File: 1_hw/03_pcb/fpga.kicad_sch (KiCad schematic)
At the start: 18 parts, among them U2 ICE40UP5K-SG48ITR

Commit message: FEAT: Added Connectors on Schematic. Created Connector Footprints.
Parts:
- gave numbers to parts that had none: 17
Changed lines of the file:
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@@
 		(on_board yes)
 		(dnp no)
-		(property "Reference" "C?"
+		(property "Reference" "C79"
 			(at 146.05 92.7162 0)
 			(effects
@@
 			(project "arb"
 				(path "/866ef9be-3b01-4288-a6e0-a2357aa17e50/13f127a8-adf3-43db-9fea-9a9f154787f6"
-					(reference "C?")
+					(reference "C79")
 					(unit 1)
 				)
@@
 		(dnp no)
 		(fields_autoplaced yes)
-		(property "Reference" "C?"
+		(property "Reference" "C84"
 			(at 180.34 78.7462 0)
 			(effects
@@
 			(project "arb"
 				(path "/866ef9be-3b01-4288-a6e0-a2357aa17e50/13f127a8-adf3-43db-9fea-9a9f154787f6"
-					(reference "C?")
+					(reference "C84")
 					(unit 1)
 				)
@@
 		(dnp no)
 		(fields_autoplaced yes)
-		(property "Reference" "U?"
+		(property "Reference" "U14"
 			(at 248.92 147.3199 0)
 			(effects
@@
 			(project ""
 				(path "/866ef9be-3b01-4288-a6e0-a2357aa17e50/13f127a8-adf3-43db-9fea-9a9f154787f6"
-					(reference "U?")
+					(reference "U14")
 					(unit 1)
 				)
@@
 		(dnp no)
 		(fields_autoplaced yes)
-		(property "Reference" "C?"
+		(property "Reference" "C81"
 			(at 170.18 78.7462 0)
 			(effects
@@
 			(project "arb"
 				(path "/866ef9be-3b01-4288-a6e0-a2357aa17e50/13f127a8-adf3-43db-9fea-9a9f154787f6"
-					(reference "C?")
+					(reference "C81")
 					(unit 1)
 				)
@@
 		(dnp no)
 		(fields_autoplaced yes)
-		(property "Reference" "C?"
+		(property "Reference" "C76"
 			(at 100.33 26.6762 0)
 			(effects
@@
 			(project "arb"
 				(path "/866ef9be-3b01-4288-a6e0-a2357aa17e50/13f127a8-adf3-43db-9fea-9a9f154787f6"
-					(reference "C?")
+					(reference "C76")
 					(unit 1)
 				)
@@
 		(on_board yes)
 		(dnp no)
-		(property "Reference" "R?"
+		(property "Reference" "R44"
 			(at 219.202 135.636 0)
 			(effects
@@
 			(project "arb"
 				(path "/866ef9be-3b01-4288-a6e0-a2357aa17e50/13f127a8-adf3-43db-9fea-9a9f154787f6"
-					(reference "R?")
+					(reference "R44")
 					(unit 1)
 				)
@@
 		(dnp no)
 		(fields_autoplaced yes)
-		(property "Reference" "C?"
+		(property "Reference" "C80"
 			(at 163.83 26.6762 0)
 			(effects
@@
 			(project "arb"
 				(path "/866ef9be-3b01-4288-a6e0-a2357aa17e50/13f127a8-adf3-43db-9fea-9a9f154787f6"
-					(reference "C?")
+					(reference "C80")
 					(unit 1)
 				)
@@
 		(on_board yes)
 		(dnp no)
-		(property "Reference" "C?"
+		(property "Reference" "C78"
 			(at 135.89 92.7162 0)
 			(effects
@@
 			(project "arb"
 				(path "/866ef9be-3b01-4288-a6e0-a2357aa17e50/13f127a8-adf3-43db-9fea-9a9f154787f6"
-					(reference "C?")
+					(reference "C78")
 					(unit 1)
 				)
@@
 		(dnp no)
 		(fields_autoplaced yes)
-		(property "Reference" "R?"
+		(property "Reference" "R42"
 			(at 182.88 83.82 90)
 			(effects
@@
 			(project "arb"
 				(path "/866ef9be-3b01-4288-a6e0-a2357aa17e50/13f127a8-adf3-43db-9fea-9a9f154787f6"
-					(reference "R?")
+					(reference "R42")
 					(unit 1)
 				)
@@
 		(dnp no)
 		(fields_autoplaced yes)
-		(property "Reference" "C?"
+		(property "Reference" "C74"
 			(at 90.17 26.6762 0)
 			(effects
@@
 			(project "arb"
 				(path "/866ef9be-3b01-4288-a6e0-a2357aa17e50/13f127a8-adf3-43db-9fea-9a9f154787f6"
-					(reference "C?")
+					(reference "C74")
 					(unit 1)
 				)
@@
 		(dnp no)
 		(fields_autoplaced yes)
-		(property "Reference" "C?"
+		(property "Reference" "C82"
 			(at 170.18 92.7162 0)
 			(effects
@@
 			(project "arb"
 				(path "/866ef9be-3b01-4288-a6e0-a2357aa17e50/13f127a8-adf3-43db-9fea-9a9f154787f6"
-					(reference "C?")
+					(reference "C82")
 					(unit 1)
 				)
@@
 		(on_board yes)
 		(dnp no)
-		(property "Reference" "R?"
+		(property "Reference" "R43"
 			(at 210.312 135.636 0)
 			(effects
@@
 			(project "arb"
 				(path "/866ef9be-3b01-4288-a6e0-a2357aa17e50/13f127a8-adf3-43db-9fea-9a9f154787f6"
-					(reference "R?")
+					(reference "R43")
 					(unit 1)
 				)
@@
 		(dnp no)
 		(fields_autoplaced yes)
-		(property "Reference" "C?"
+		(property "Reference" "C86"
 			(at 247.65 128.2763 0)
 			(effects
@@
 			(project "arb"
 				(path "/866ef9be-3b01-4288-a6e0-a2357aa17e50/13f127a8-adf3-43db-9fea-9a9f154787f6"
-					(reference "C?")
+					(reference "C86")
 					(unit 1)
 				)
@@
 		(dnp no)
 		(fields_autoplaced yes)
-		(property "Reference" "C?"
+		(property "Reference" "C85"
 			(at 180.34 92.7162 0)
 			(effects
@@
 			(project "arb"
 				(path "/866ef9be-3b01-4288-a6e0-a2357aa17e50/13f127a8-adf3-43db-9fea-9a9f154787f6"
-					(reference "C?")
+					(reference "C85")
 					(unit 1)
 				)
@@
 		(dnp no)
 		(fields_autoplaced yes)
-		(property "Reference" "C?"
+		(property "Reference" "C75"
 			(at 91.44 104.1462 0)
 			(effects
@@
 			(project "arb"
 				(path "/866ef9be-3b01-4288-a6e0-a2357aa17e50/13f127a8-adf3-43db-9fea-9a9f154787f6"
-					(reference "C?")
+					(reference "C75")
 					(unit 1)
 				)
@@
 		(dnp no)
 		(fields_autoplaced yes)
-		(property "Reference" "C?"
+		(property "Reference" "C83"
 			(at 173.99 26.6762 0)
 			(effects
@@
 			(project "arb"
 				(path "/866ef9be-3b01-4288-a6e0-a2357aa17e50/13f127a8-adf3-43db-9fea-9a9f154787f6"
-					(reference "C?")
+					(reference "C83")
 					(unit 1)
 				)
@@
 		(dnp no)
 		(fields_autoplaced yes)
-		(property "Reference" "C?"
+		(property "Reference" "C77"
 			(at 101.6 104.1462 0)
 			(effects
@@
 			(project "arb"
 				(path "/866ef9be-3b01-4288-a6e0-a2357aa17e50/13f127a8-adf3-43db-9fea-9a9f154787f6"
-					(reference "C?")
+					(reference "C77")
 					(unit 1)
 				)

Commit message: FEAT: Assigned Reference Designators; Assigned Passives Part Numbers & Footprints (0603); Assigned LCSC P/Ns.
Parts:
- C59: renamed from C74; footprint (none) -> Capacitor_SMD:C_0603_1608Metric; LCSC (none) -> C24452; Part Number (none) -> CL10B104JB8NNNC
- C60: renamed from C75; footprint (none) -> Capacitor_SMD:C_0603_1608Metric; LCSC (none) -> C24452; Part Number (none) -> CL10B104JB8NNNC
- C61: renamed from C76; footprint (none) -> Capacitor_SMD:C_0603_1608Metric; LCSC (none) -> C1705; Part Number (none) -> CL10A475KP8NNNC
- C62: renamed from C77; footprint (none) -> Capacitor_SMD:C_0603_1608Metric; LCSC (none) -> C1705; Part Number (none) -> CL10A475KP8NNNC
- C63: renamed from C78; footprint (none) -> Capacitor_SMD:C_0603_1608Metric; LCSC (none) -> C1705; Part Number (none) -> CL10A475KP8NNNC
- C64: renamed from C79; footprint (none) -> Capacitor_SMD:C_0603_1608Metric; LCSC (none) -> C24452; Part Number (none) -> CL10B104JB8NNNC
- C65: renamed from C80; footprint (none) -> Capacitor_SMD:C_0603_1608Metric; LCSC (none) -> C24452; Part Number (none) -> CL10B104JB8NNNC
- C66: renamed from C81; footprint (none) -> Capacitor_SMD:C_0603_1608Metric; LCSC (none) -> C24452; Part Number (none) -> CL10B104JB8NNNC
- C67: renamed from C82; footprint (none) -> Capacitor_SMD:C_0603_1608Metric; LCSC (none) -> C24452; Part Number (none) -> CL10B104JB8NNNC
- C68: renamed from C83; footprint (none) -> Capacitor_SMD:C_0603_1608Metric; LCSC (none) -> C1705; Part Number (none) -> CL10A475KP8NNNC
- C69: renamed from C84; footprint (none) -> Capacitor_SMD:C_0603_1608Metric; LCSC (none) -> C1705; Part Number (none) -> CL10A475KP8NNNC
- C70: renamed from C85; footprint (none) -> Capacitor_SMD:C_0603_1608Metric; LCSC (none) -> C1705; Part Number (none) -> CL10A475KP8NNNC
- C71: renamed from C86; LCSC (none) -> C24452; PN CL10B104JB8NNNC -> (none); Part Number (none) -> CL10B104JB8NNNC
- R33: renamed from R42; footprint (none) -> Resistor_SMD:R_0603_1608Metric; LCSC (none) -> C105588; Part Number (none) -> RC0603FR-07100RL
- R34: renamed from R43; LCSC (none) -> C25804; PN CR-03FC7---10K -> (none); Part Number (none) -> 0603WAF1002T5E
- R35: renamed from R44; LCSC (none) -> C25804; PN CR-03FC7---10K -> (none); Part Number (none) -> 0603WAF1002T5E
- U12: renamed from U2; LCSC (none) -> C2678152; Part Number (none) -> ICE40UP5K-SG48I
- U13: renamed from U14; LCSC (none) -> C97521

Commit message: FEAT: Added MCU Flash. Finished creating & assigning footprints. Ran ERC & cleared out issues. Ready for Layout.
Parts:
- removed C71: 100n, Capacitor_SMD:C_0603_1608Metric, symbol Device:C_Small
- removed U13: W25Q128JVSIQ, Package_SO:SOIC-8_5.23x5.23mm_P1.27mm, symbol BRZK_MEMORY:W25Q128JVSIQ
- added D4, D5, D6: LED, LED_SMD:LED_1206_3216Metric, symbol Device:LED
- added R36: 220, Resistor_SMD:R_0603_1608Metric, symbol Device:R_Small_US
- R34, R35: value 10k -> 220; LCSC C25804 -> C22962; Part Number 0603WAF1002T5E -> 0603WAF2200T5E
- renumbered R33 to R37
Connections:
- net 3P3V_D: now also R34.1, R35.1, R36.1; no longer R34.2, R35.2
- net GPIO_LED0_FPGA_LED_OD: now also D4.1 (K)
- net GPIO_LED1_FPGA_LED_OD: now also D5.1 (K)
- net GPIO_LED2_FPGA_LED_OD: now also D6.1 (K)
- net SPI_CS_MCU_FPGA_3P3_L: no longer R35.1
- net SPI_SCLK_MCU_FPGA_3P3: no longer R34.1
- new net: D4.2 (A), R34.2
- new net: D5.2 (A), R35.2
- new net: D6.2 (A), R36.2
- no-connect marks 16 -> 14
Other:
- moved on the sheet: C63, C64, C65, C66, C67, C68, C69, C70, R37, U12C, U12D

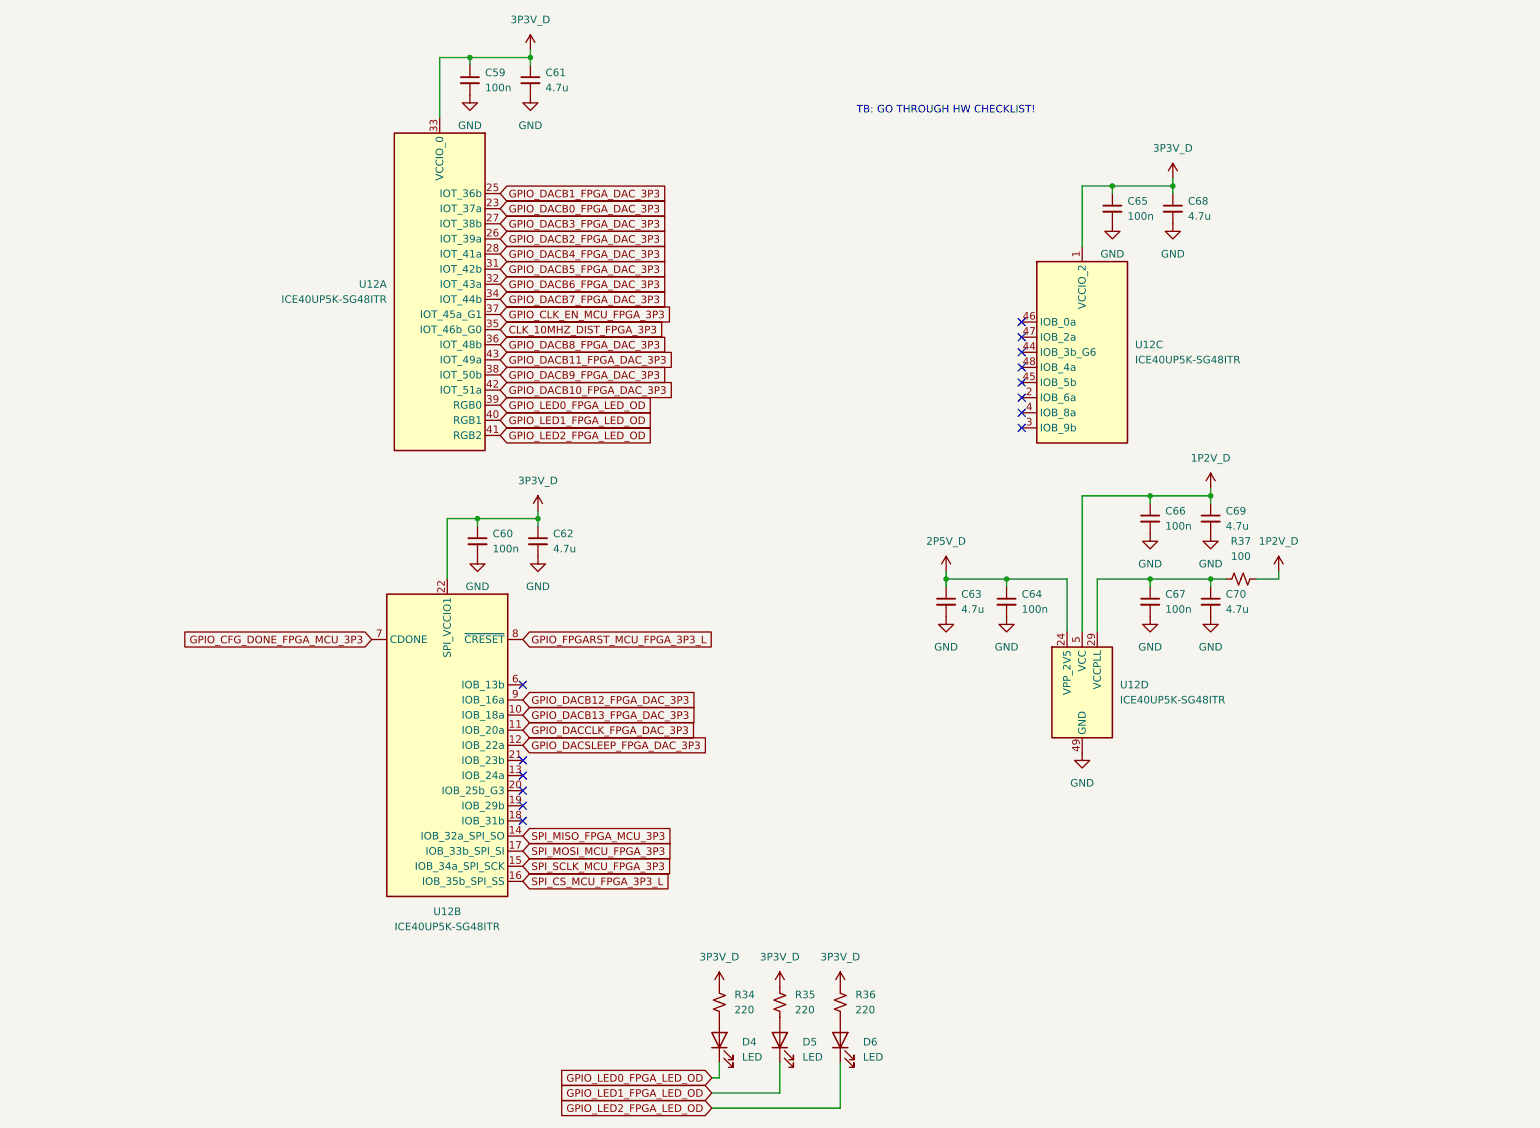
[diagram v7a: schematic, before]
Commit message: MINOR: Verified Footprints to Datasheets. Added Pull Ups on FPGA DONE/Config/SPI Chip Select Pins.
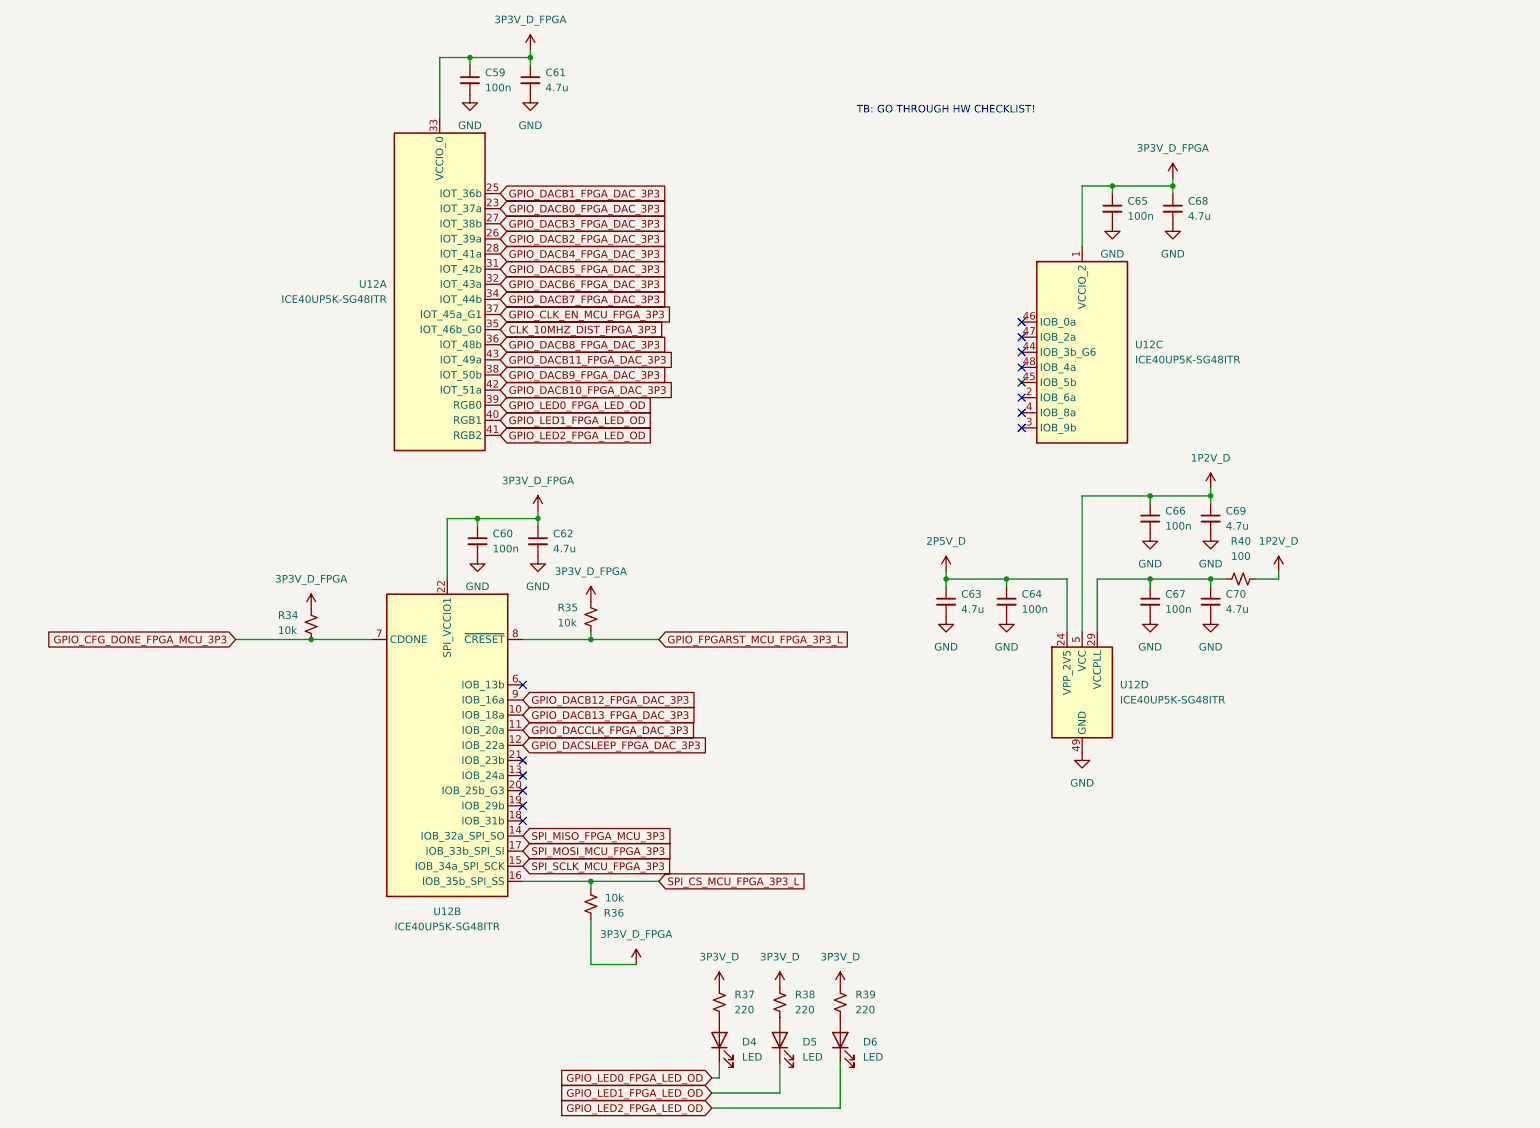
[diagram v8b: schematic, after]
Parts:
- added R34, R35, R36: 10k, Resistor_SMD:R_0603_1608Metric, symbol Device:R_Small_US
- renumbered R34 to R37, R35 to R38, R36 to R39, R37 to R40
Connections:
- net 3P3V_D: no longer C59.1, C60.1, C61.1, C62.1, C65.1, C68.1, U12.1 (VCCIO_2), U12.22 (SPI_VCCIO1), U12.33 (VCCIO_0)
- net GPIO_CFG_DONE_FPGA_MCU_3P3: now also R34.1
- net GPIO_FPGARST_MCU_FPGA_3P3_L: now also R35.1
- net SPI_CS_MCU_FPGA_3P3_L: now also R36.1
- new net 3P3V_D_FPGA: C59.1, C60.1, C61.1, C62.1, C65.1, C68.1, R34.2, R35.2, R36.2, U12.1 (VCCIO_2), U12.22 (SPI_VCCIO1), U12.33 (VCCIO_0)
